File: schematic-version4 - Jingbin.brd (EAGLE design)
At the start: 47 x 28 mm, 54 parts, among them J2 FTDI_DEVICE, M1 WIRELESS-NRF24L01, Q1 NX3225GD, T1 NMOS, T2 NMOS, T3 NMOS, T4 NMOS, U1 ATMEGA328P_TQFP, U2 GY-521MPU6050

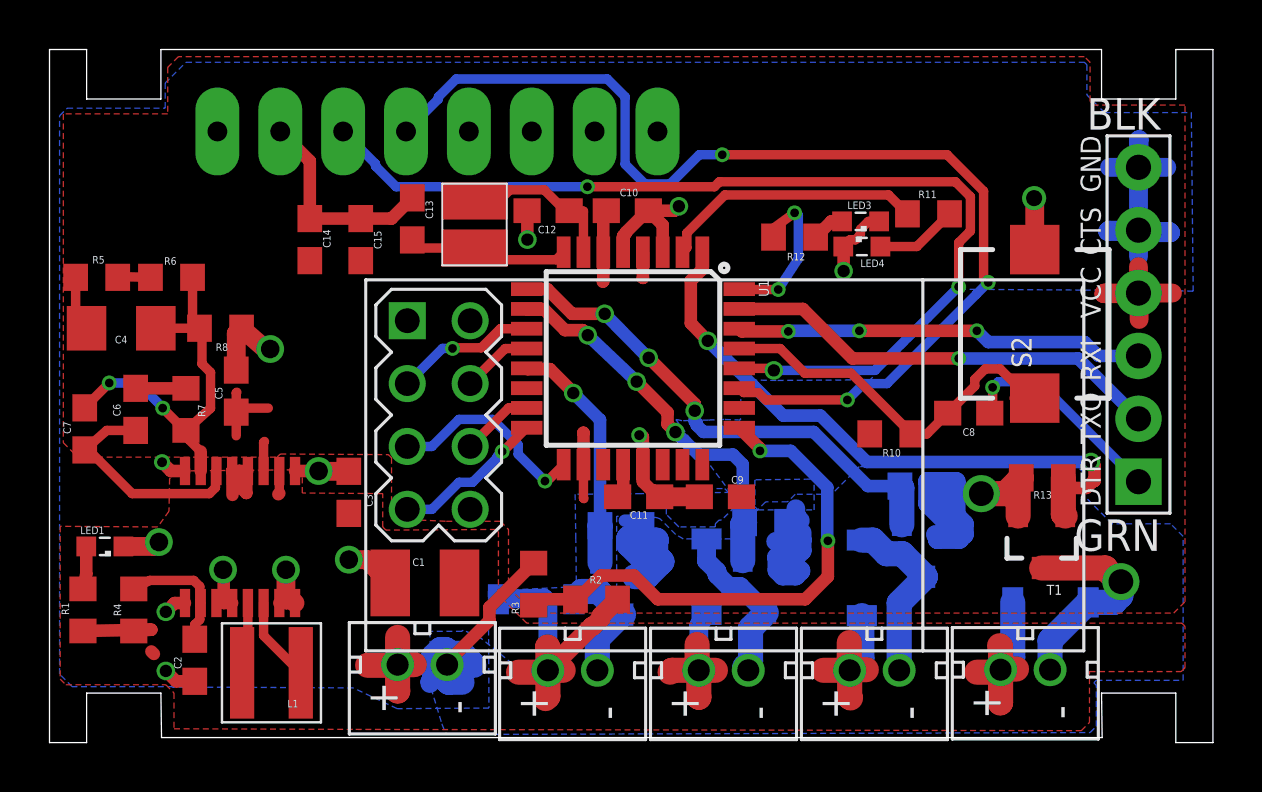
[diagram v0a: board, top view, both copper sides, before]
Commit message: More paths, hopefully less bottleneck
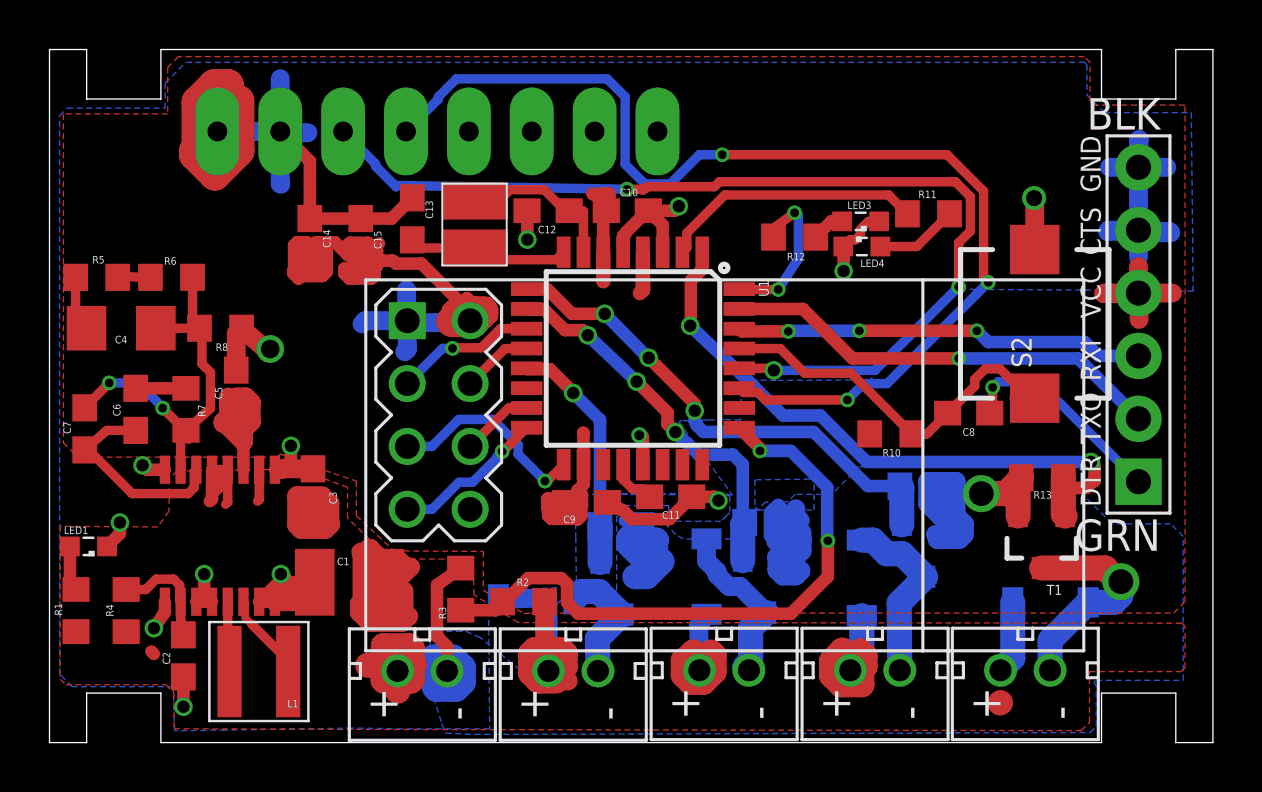
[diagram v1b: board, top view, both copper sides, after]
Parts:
- moved C9 5.42 mm to (21.7, 9.70), turned to 0 degrees
- moved C1 3.05 mm to (12.1, 6.48)
- moved R3 2.95 mm to (16.6, 6.20)
- moved R2 2.95 mm to (19.2, 5.69)
- moved C3 1.45 mm to (10.6, 10.2)
- moved C11 1.30 mm to (25.1, 9.93)
- moved U$2 0.81 mm to (6.88, 8.36)
- moved LED1 0.66 mm to (1.57, 7.92)
- moved L1 0.51 mm to (8.46, 2.87)
- moved C2 0.49 mm to (5.41, 3.51)
- moved R4 0.31 mm to (3.10, 5.33)
- moved R1 0.28 mm to (1.07, 5.34)
- moved U$1 0.25 mm to (15.1, 2.90)
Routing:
- net V_REG_OUT: track 18.6 -> 64.0 mm
- net GND: track 92.5 -> 108.9 mm
- net PWR: track 46.5 -> 61.8 mm
- net V_BAT: track 21.4 -> 25.3 mm
- net N$16: track 5.44 -> 4.46 mm
- net N$19: track 9.16 -> 8.37 mm
- net N$25: track 1.39 -> 1.96 mm
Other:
- outline, holes or cut-outs redrawn

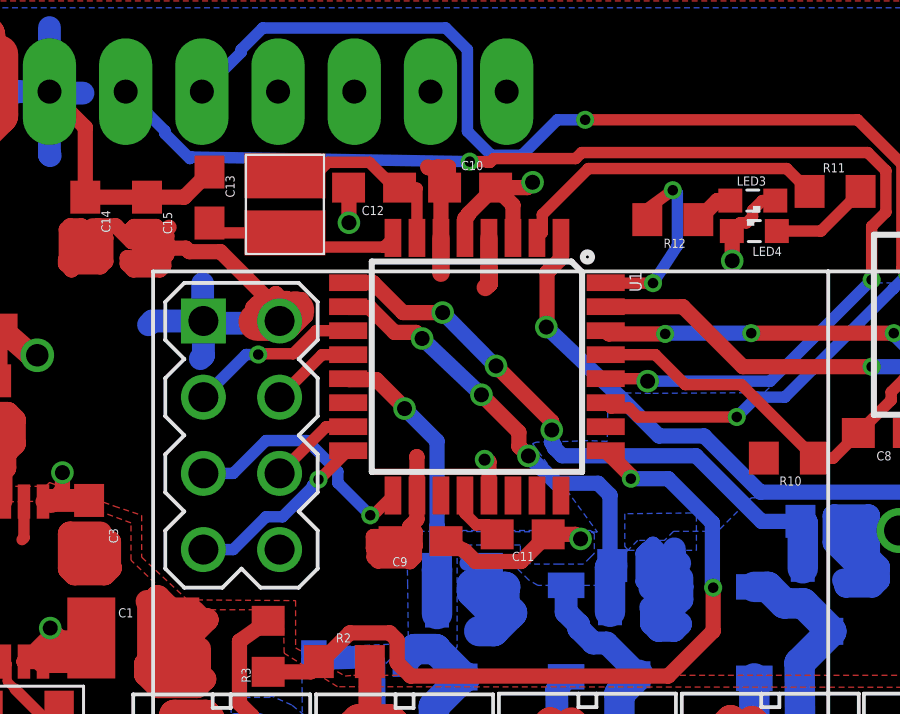
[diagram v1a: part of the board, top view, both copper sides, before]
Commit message: Slightly adjusted trace thickness
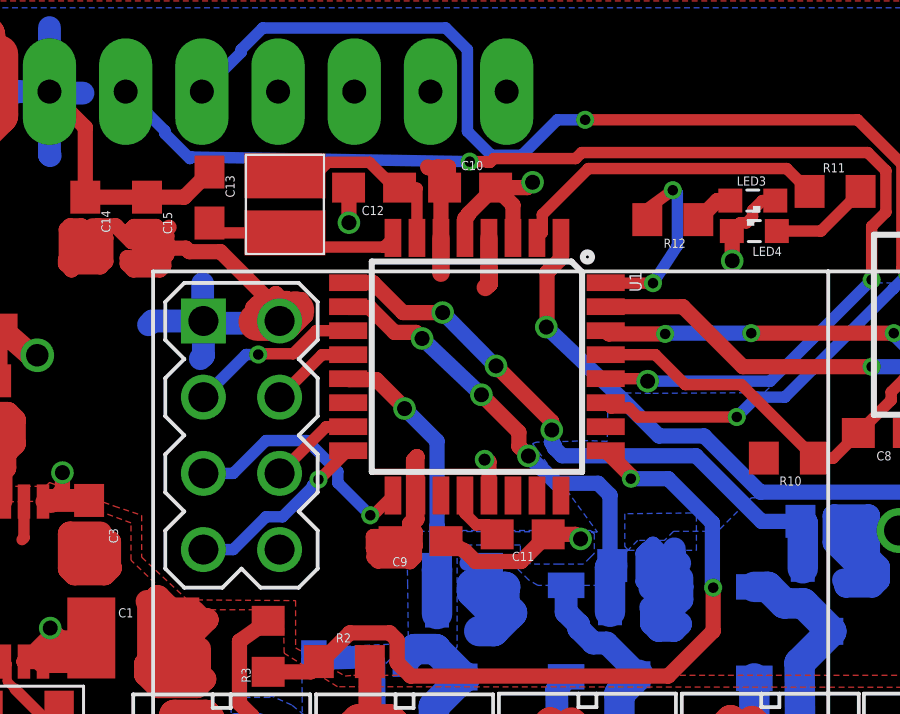
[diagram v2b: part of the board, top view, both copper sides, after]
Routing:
- net V_REG_OUT: track 64.0 -> 67.5 mm
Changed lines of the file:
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@@
 <vertex x="9.3218" y="11.6586"/>
 </polygon>
-<wire x1="22.3712" y1="21.367" x2="22.4926" y2="21.4884" width="0.381" layer="1"/>
-<wire x1="22.3712" y1="19.812" x2="22.3712" y2="21.367" width="0.508" layer="1"/>
 <wire x1="2.755" y1="18.796" x2="2.9836" y2="18.8214" width="0.381" layer="1"/>
 <wire x1="2.9836" y1="18.8214" x2="4.0776" y2="18.796" width="0.381" layer="1"/>
@@
 <wire x1="23.9712" y1="18.2816" x2="23.8506" y2="18.161" width="0.5842" layer="1"/>
 <wire x1="23.9712" y1="18.2816" x2="23.9776" y2="18.288" width="0.5842" layer="1"/>
-<wire x1="23.9776" y1="18.288" x2="23.9776" y2="18.7706" width="0.5842" layer="1"/>
+<wire x1="23.9776" y1="18.7706" x2="23.9776" y2="18.288" width="0.5842" layer="1"/>
 <wire x1="21.3301" y1="10.1913" x2="21.5712" y2="10.4324" width="0.508" layer="1"/>
 <wire x1="21.5712" y1="10.4324" x2="21.5712" y2="11.2268" width="0.508" layer="1"/>
@@
 <wire x1="7.9296" y1="13.9652" x2="7.56525" y2="13.9652" width="0.762" layer="1"/>
 <wire x1="8.1534" y1="13.7414" x2="7.9296" y2="13.9652" width="0.762" layer="1"/>
+<wire x1="21.3301" y1="10.1913" x2="21.3301" y2="10.2965625" width="0.508" layer="1"/>
+<wire x1="21.3301" y1="10.2965625" x2="21.457" y2="10.4234625" width="0.508" layer="1"/>
+<wire x1="21.457" y1="12.4014" x2="21.5712" y2="12.5156" width="0.508" layer="1"/>
+<wire x1="21.457" y1="10.4234625" x2="21.457" y2="12.4014" width="0.508" layer="1"/>
+<wire x1="22.4926" y1="21.4884" x2="22.3712" y2="21.367" width="0.508" layer="1"/>
+<wire x1="22.3712" y1="21.367" x2="22.3712" y2="19.812" width="0.508" layer="1"/>
+<wire x1="23.9712" y1="19.812" x2="23.9776" y2="19.8056" width="0.508" layer="1"/>
+<wire x1="23.9776" y1="19.8056" x2="23.9776" y2="18.7706" width="0.508" layer="1"/>
 </signal>
 <signal name="V_BAT">

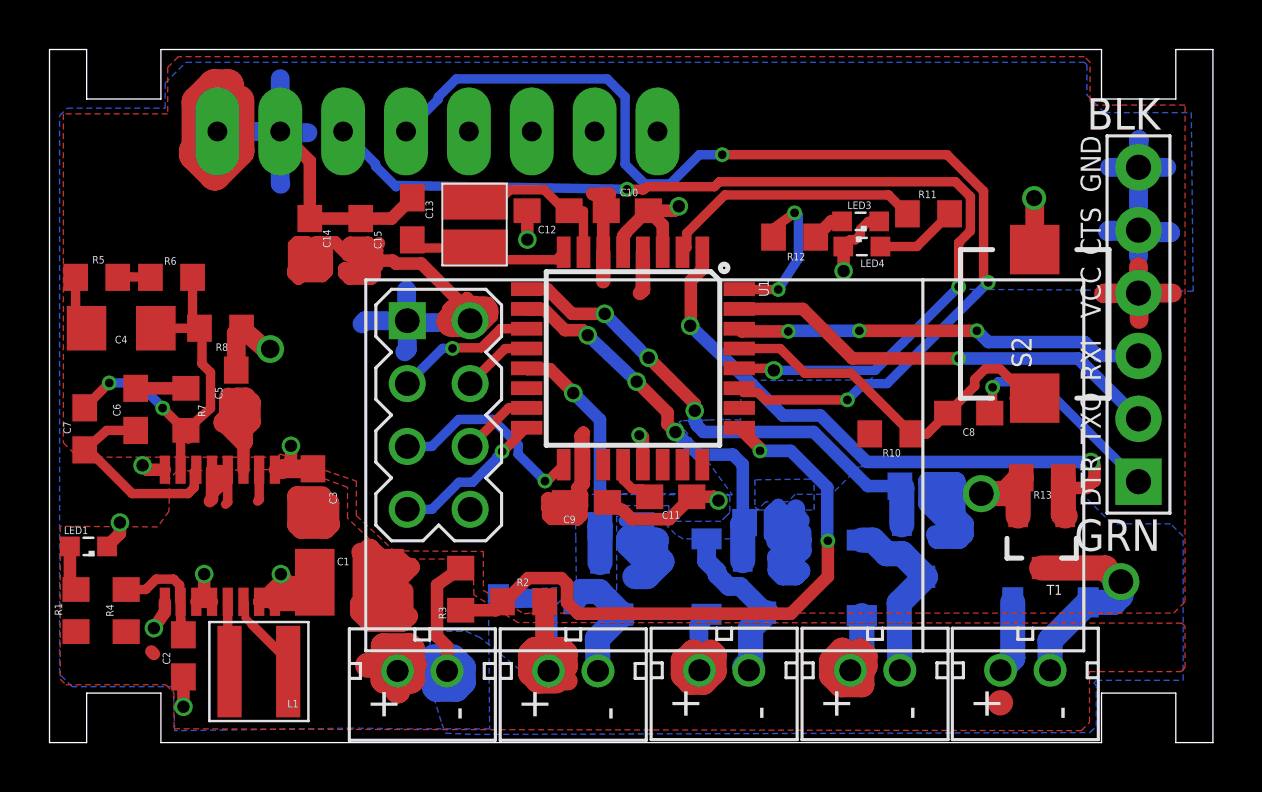
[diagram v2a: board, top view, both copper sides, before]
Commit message: Moved radio decoupling capacitor closer to radio power
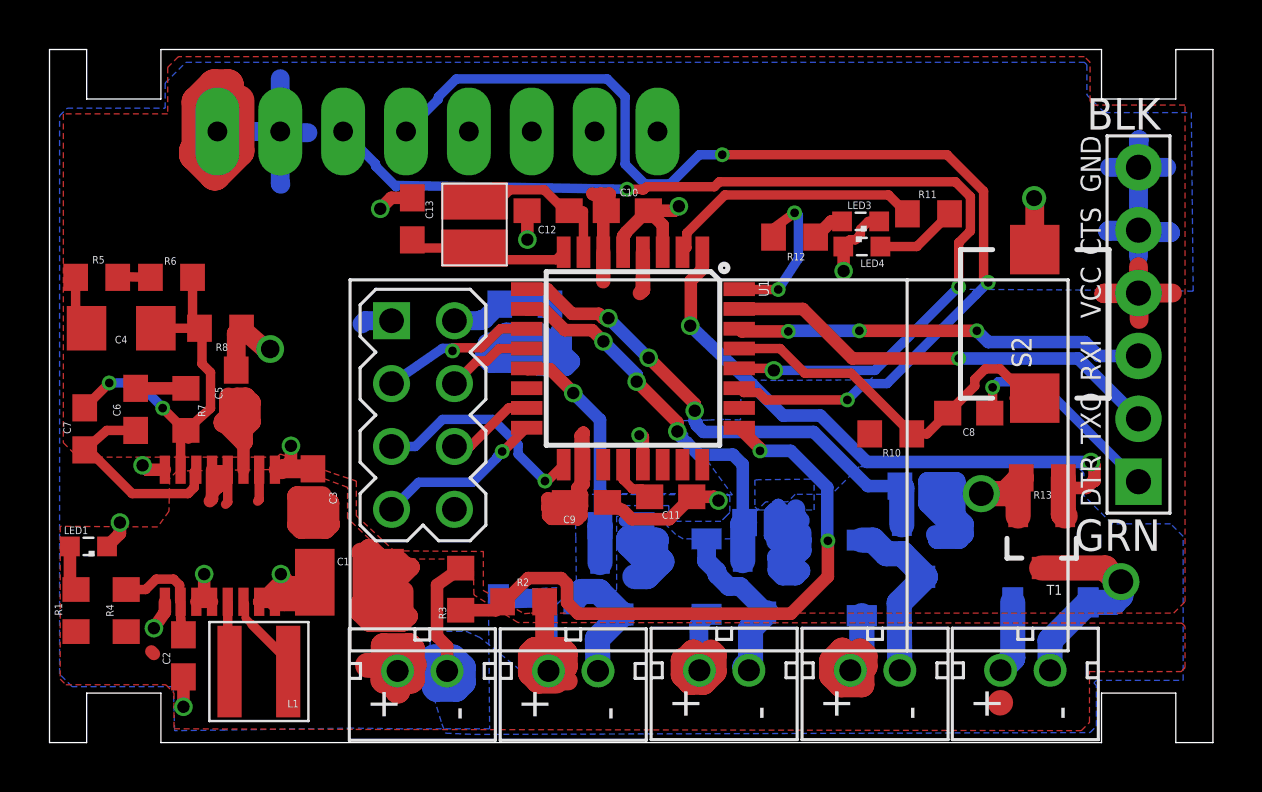
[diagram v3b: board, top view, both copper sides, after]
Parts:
- moved C14 8.41 mm to (18.2, 16.9), flipped to the bottom, turned to 270 degrees
- moved C15 8.39 mm to (20.2, 16.9), flipped to the bottom, turned to 270 degrees
- moved M1 0.63 mm to (26.5, 10.7)
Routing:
- net V_REG_OUT: track 67.5 -> 46.9 mm
- net GND: track 108.9 -> 107.4 mm, vias 15 -> 16
- net MISO: track 6.22 -> 6.85 mm
- net SCK: track 8.30 -> 8.93 mm
- net MOSI: track 2.93 -> 3.57 mm
- net CSN: track 2.87 -> 3.51 mm
- net CE: track 5.74 -> 6.37 mm

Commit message: More finer adjustments
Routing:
- net V_REG_OUT: track 46.9 -> 52.7 mm
- net GND: track 107.4 -> 111.1 mm
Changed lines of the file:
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@@
 <wire x1="19.5326" y1="15.4686" x2="19.812" y2="15.1892" width="0.762" layer="16"/>
 <wire x1="19.812" y1="15.1892" x2="20.8534" y2="15.1892" width="0.762" layer="16"/>
+<wire x1="13.8176" y1="17.0434" x2="13.8176" y2="18.288" width="0.762" layer="16"/>
+<wire x1="13.8176" y1="18.288" x2="13.7922" y2="18.3134" width="0.762" layer="16"/>
+<wire x1="13.8176" y1="17.0434" x2="13.7922" y2="17.018" width="0.762" layer="16"/>
+<wire x1="13.7922" y1="17.018" x2="13.7922" y2="15.7988" width="0.762" layer="16"/>
+<wire x1="13.8176" y1="17.0434" x2="13.8684" y2="17.0942" width="0.762" layer="16"/>
+<wire x1="13.8684" y1="17.0942" x2="15.0114" y2="17.0942" width="0.762" layer="16"/>
 </signal>
 <signal name="SDA">
@@
 <wire x1="17.46545625" y1="17.099" x2="17.40985625" y2="17.0434" width="0.762" layer="16"/>
 <wire x1="17.40985625" y1="17.0434" x2="16.3576" y2="17.0434" width="0.762" layer="16"/>
+<wire x1="16.3576" y1="17.0434" x2="16.3576" y2="18.1864" width="0.762" layer="1"/>
+<wire x1="16.3576" y1="18.1864" x2="15.6972" y2="17.526" width="0.762" layer="1"/>
+<wire x1="15.6972" y1="17.526" x2="15.6718" y2="17.526" width="0.762" layer="1"/>
+<wire x1="15.6718" y1="16.6116" x2="15.7734" y2="16.51" width="0.762" layer="1"/>
+<wire x1="15.7734" y1="16.51" x2="15.7857625" y2="16.51" width="0.762" layer="1"/>
+<wire x1="16.08691875" y1="16.6744" x2="16.154040625" y2="16.719146875" width="0.762" layer="1"/>
+<wire x1="16.154040625" y1="16.719146875" x2="16.377778125" y2="16.6744" width="0.762" layer="1"/>
+<wire x1="15.7857625" y1="16.51" x2="15.9501625" y2="16.6744" width="0.762" layer="1"/>
+<wire x1="15.9501625" y1="16.6744" x2="16.08691875" y2="16.6744" width="0.762" layer="1"/>
+<wire x1="16.377778125" y1="16.6744" x2="16.9418" y2="16.6744" width="0.762" layer="1"/>
+<wire x1="16.9418" y1="16.6744" x2="16.9418" y2="16.9926" width="0.762" layer="1"/>
+<wire x1="16.9418" y1="16.9926" x2="17.272" y2="17.3228" width="0.762" layer="1"/>
+<wire x1="17.272" y1="17.3228" x2="16.9418" y2="17.653" width="0.762" layer="1"/>
+<wire x1="16.9418" y1="17.653" x2="16.9418" y2="17.8054" width="0.762" layer="1"/>
+<wire x1="15.6718" y1="17.526" x2="15.6718" y2="16.6116" width="0.762" layer="1"/>
 </signal>
 <signal name="V_BAT">

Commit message: I swear it's the last time
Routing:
- net V_REG_OUT: track 52.7 -> 53.7 mm
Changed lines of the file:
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@@
 <wire x1="23.9712" y1="19.812" x2="23.9776" y2="19.8056" width="0.508" layer="1"/>
 <wire x1="23.9776" y1="19.8056" x2="23.9776" y2="18.7706" width="0.508" layer="1"/>
-<wire x1="20.2184" y1="17.7156" x2="18.1864" y2="17.7156" width="0.762" layer="16"/>
-<wire x1="18.1864" y1="17.7156" x2="17.5698" y2="17.099" width="0.762" layer="16"/>
-<wire x1="17.5698" y1="17.099" x2="17.46545625" y2="17.099" width="0.762" layer="16"/>
-<wire x1="17.46545625" y1="17.099" x2="17.40985625" y2="17.0434" width="0.762" layer="16"/>
 <wire x1="17.40985625" y1="17.0434" x2="16.3576" y2="17.0434" width="0.762" layer="16"/>
 <wire x1="16.3576" y1="17.0434" x2="16.3576" y2="18.1864" width="0.762" layer="1"/>
@@
 <wire x1="16.9418" y1="17.653" x2="16.9418" y2="17.8054" width="0.762" layer="1"/>
 <wire x1="15.6718" y1="17.526" x2="15.6718" y2="16.6116" width="0.762" layer="1"/>
+<wire x1="20.2184" y1="17.7156" x2="18.1864" y2="17.7156" width="1.016" layer="16"/>
+<wire x1="18.1864" y1="17.7156" x2="17.90245625" y2="17.7156" width="1.016" layer="16"/>
+<wire x1="17.90245625" y1="17.7156" x2="17.35725625" y2="17.1704" width="1.016" layer="16"/>
+<wire x1="17.35725625" y1="17.1704" x2="17.2470375" y2="17.1704" width="1.016" layer="16"/>
+<wire x1="17.2470375" y1="17.1704" x2="17.1200375" y2="17.0434" width="1.016" layer="16"/>
+<wire x1="17.1200375" y1="17.0434" x2="16.3576" y2="17.0434" width="1.016" layer="16"/>
 </signal>
 <signal name="V_BAT">

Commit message: More paths...
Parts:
- moved M1 0.79 mm to (26.5, 11.5)
- moved Q1 0.59 mm to (16.6, 21.0)
- moved C12 0.58 mm to (19.6, 21.5)
- moved C13 0.55 mm to (14.1, 21.3)
- moved C10 0.39 mm to (23.4, 21.1), turned to 180 degrees
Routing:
- net GND: track 111.1 -> 113.8 mm, vias 16 -> 17
- net SCL: track 40.9 -> 42.2 mm
- net V_REG_OUT: track 53.7 -> 54.9 mm
- net SDA: track 44.7 -> 45.6 mm
- net CE: track 6.37 -> 6.05 mm, vias 1 -> 0
